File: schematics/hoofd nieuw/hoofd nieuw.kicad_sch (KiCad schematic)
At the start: 39 parts, among them J1 Conn_01x04_Pin, J2 Conn_01x02_Pin, J3 SFR02, J4 Conn_01x04_Pin, U1 ATtiny402-SS, U2 BH1750FVI-TR, U3 BH1750FVI-TR, Y1 ECS-2333MV-xxx-xx

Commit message: plaats de componenten grofweg
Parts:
- removed J4: Conn_01x04_Pin, Connector_PinHeader_2.54mm:PinHeader_1x04_P2.54mm_Vertical, symbol Connector:Conn_01x04_Pin
- added J4: Conn_01x03_Pin, Connector_PinHeader_2.54mm:PinHeader_1x03_P2.54mm_Vertical, symbol Connector:Conn_01x03_Pin
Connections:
- net +3.3V: now also C1.1, U1.1 (VCC), J4.3 (Pin_3)
- net GND: now also J4.1 (Pin_1)
- net UPDI/~{RESET}: now also J4.2 (Pin_2)
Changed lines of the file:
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@@
 	)
 	(junction
+		(at 57.15 54.61)
+		(diameter 0)
+		(color 255 0 0 1)
+	)
+	(junction
 		(at 137.16 138.43)
 		(diameter 0)
@@
 	(wire
 		(pts
-			(xy 50.8 54.61) (xy 54.61 54.61)
+			(xy 50.8 54.61) (xy 57.15 54.61)
 		)
 		(stroke
@@
 	(wire
 		(pts
+			(xy 57.15 53.34) (xy 57.15 54.61)
+		)
+		(stroke
+			(width 0)
+			(type default)
+			(color 255 0 0 1)
+		)
+	)
+	(wire
+		(pts
 			(xy 106.68 53.34) (xy 106.68 54.61)
 		)
@@
 	(wire
 		(pts
-			(xy 57.15 53.34) (xy 57.15 63.5)
+			(xy 57.15 54.61) (xy 57.15 63.5)
 		)
 		(stroke
@@
 	(wire
 		(pts
-			(xy 54.61 54.61) (xy 54.61 53.34)
-		)
-		(stroke
-			(width 0)
-			(type default)
-			(color 255 0 0 1)
-		)
-	)
-	(wire
-		(pts
 			(xy 96.52 182.88) (xy 87.63 182.88)
 		)
@@
 	)
 	(symbol
-		(lib_id "Connector:Conn_01x04_Pin")
-		(at 59.69 48.26 270)
-		(unit 1)
-		(exclude_from_sim no)
-		(in_bom yes)
-		(on_board yes)
-		(dnp no)
-		(fields_autoplaced yes)
-		(property "Reference" "J4"
-			(at 58.42 43.18 90)
-			(effects
-				(font
-					(size 1.27 1.27)
-				)
-			)
-		)
-		(property "Value" "Conn_01x04_Pin"
-			(at 58.42 45.72 90)
-			(effects
-				(font
-					(size 1.27 1.27)
-				)
-			)
-		)
-		(property "Footprint" "Connector_PinHeader_2.54mm:PinHeader_1x04_P2.54mm_Vertical"
-			(at 59.69 48.26 0)
-			(effects
-				(font
-					(size 1.27 1.27)
-				)
-				(hide yes)
-			)
-		)
-		(property "Datasheet" "~"
-			(at 59.69 48.26 0)
-			(effects
-				(font
-					(size 1.27 1.27)
-				)
-				(hide yes)
-			)
-		)
-		(property "Description" "Generic connector, single row, 01x04, script generated"
-			(at 59.69 48.26 0)
-			(effects
-				(font
-					(size 1.27 1.27)
-				)
-				(hide yes)
-			)
-		)
-		(pin "3"
-		)
-		(pin "1"
-		)
-		(pin "4"
-		)
-		(pin "2"
-		)
-		(instances
-			(project "hoofd nieuw"
-				(path "/7e0a6d27-e85c-4a07-8035-4491285a0fea"
-					(reference "J4")
-					(unit 1)
-				)
-			)
-		)
-	)
-	(symbol
 		(lib_id "power:GND")
 		(at 214.63 116.84 0)
@@
 					(unit 1)
 				)
+			)
+		)
+	)
+	(symbol
+		(lib_id "Connector:Conn_01x03_Pin")
+		(at 59.69 48.26 270)
+		(unit 1)
+		(exclude_from_sim no)
+		(in_bom yes)
+		(on_board yes)
+		(dnp no)
+		(fields_autoplaced yes)
+		(property "Reference" "J4"
+			(at 59.69 43.18 90)
+			(effects
+				(font
+					(size 1.27 1.27)
+				)
+			)
+		)
+		(property "Value" "Conn_01x03_Pin"
+			(at 59.69 45.72 90)
+			(effects
+				(font
+					(size 1.27 1.27)
+				)
+			)
+		)
+		(property "Footprint" "Connector_PinHeader_2.54mm:PinHeader_1x03_P2.54mm_Vertical"
+			(at 59.69 48.26 0)
+			(effects
+				(font
+					(size 1.27 1.27)
+				)
+				(hide yes)
+			)
+		)
+		(property "Datasheet" "~"
+			(at 59.69 48.26 0)
+			(effects
+				(font
+					(size 1.27 1.27)
+				)
+				(hide yes)
+			)
+		)
+		(property "Description" "Generic connector, single row, 01x03, script generated"
+			(at 59.69 48.26 0)
+			(effects
+				(font
+					(size 1.27 1.27)
+				)
+				(hide yes)
+			)
+		)
+		(pin "1"
+		)
+		(pin "2"
+		)
+		(pin "3"
+		)
+		(instances
+			(project ""
+				(path "/7e0a6d27-e85c-4a07-8035-4491285a0fea"
+					(reference "J4")
+					(unit 1)
+				)

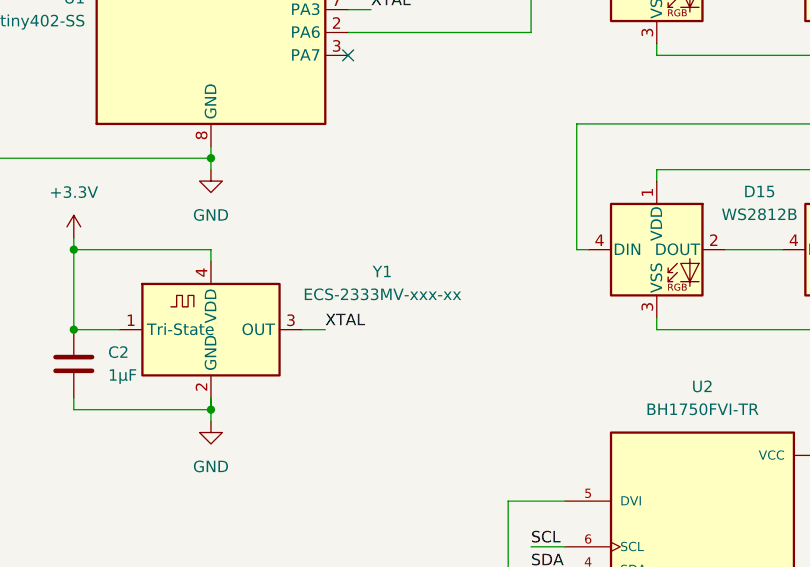
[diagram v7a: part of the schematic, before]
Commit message: voeg de ontbrekende foodprints toe
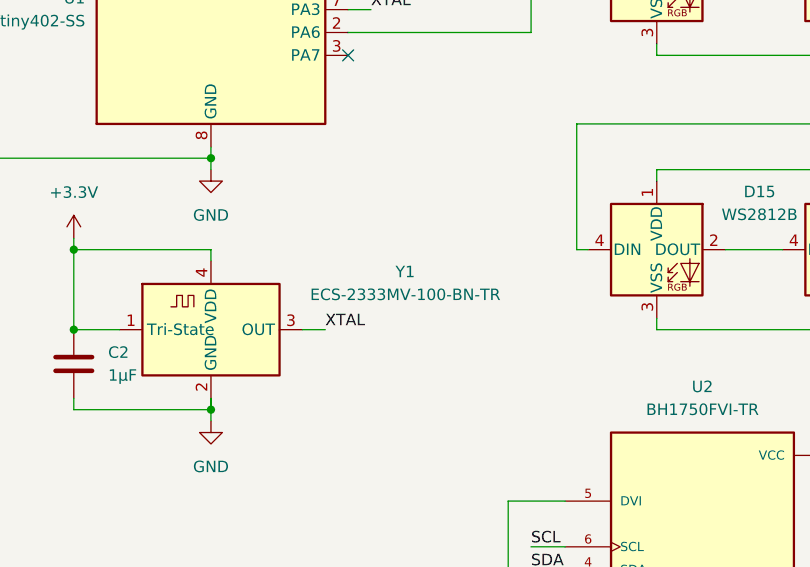
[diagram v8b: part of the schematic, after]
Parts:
- Y1: value ECS-2333MV-xxx-xx -> ECS-2333MV-100-BN-TR; footprint Oscillator:Oscillator_SMD_ECS_2333MV-xxx-xx-4Pin_2.5x3.2mm -> Oscillator:ESC-2333-xxx-xxx
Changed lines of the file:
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@@
 		(fields_autoplaced yes)
 		(property "Reference" "Y1"
-			(at 76.2 109.1498 0)
+			(at 78.74 109.1498 0)
 			(effects
 				(font
@@
 			)
 		)
-		(property "Value" "ECS-2333MV-xxx-xx"
-			(at 76.2 111.6898 0)
+		(property "Value" "ECS-2333MV-100-BN-TR"
+			(at 78.74 111.6898 0)
 			(effects
 				(font
@@
 			)
 		)
-		(property "Footprint" "Oscillator:Oscillator_SMD_ECS_2333MV-xxx-xx-4Pin_2.5x3.2mm"
+		(property "Footprint" "Oscillator:ESC-2333-xxx-xxx"
 			(at 65.278 133.604 0)
 			(effects
